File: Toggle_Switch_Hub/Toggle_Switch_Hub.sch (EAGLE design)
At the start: 6 parts

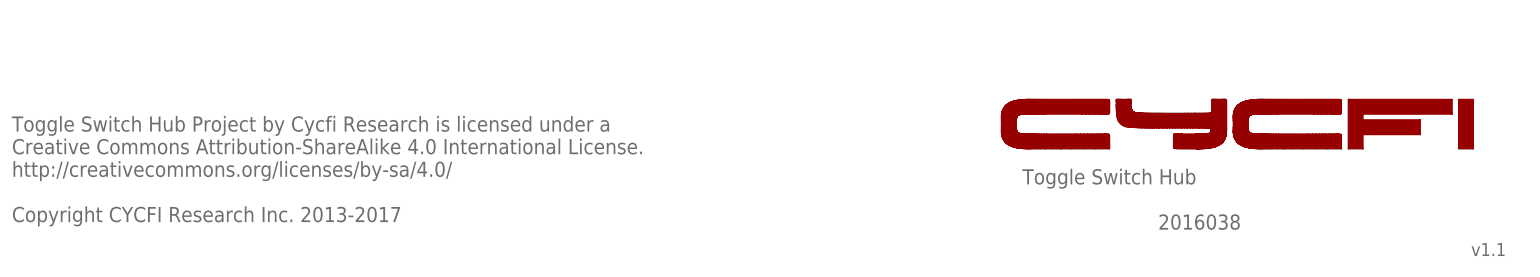
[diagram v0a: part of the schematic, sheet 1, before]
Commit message: Updated BOM and Document Number
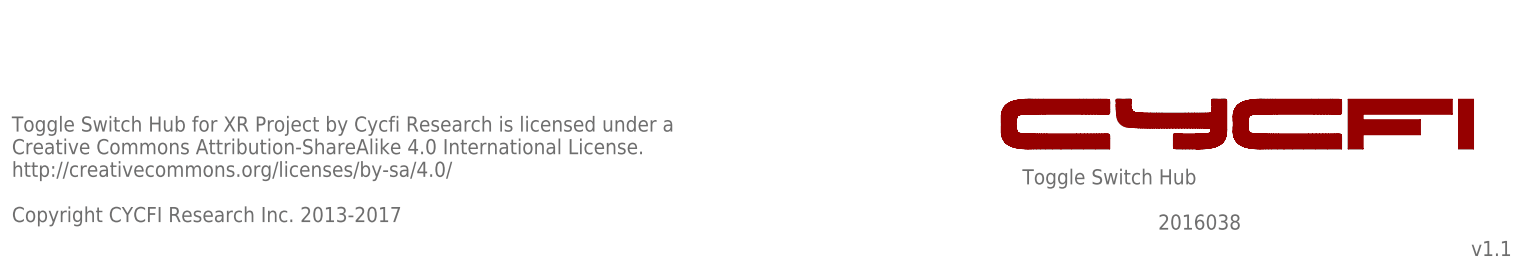
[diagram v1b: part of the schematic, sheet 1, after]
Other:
- note added: "Toggle Switch Hub for XR Project by Cycfi Research is licensed under a Creative Commons Attribution-ShareAlike 4.0 International License. http://creativecommons.org/licenses/by-sa/4.0/ Copyright CYCFI Research Inc. 2013-2017"
- note removed: "Toggle Switch Hub Project by Cycfi Research is licensed under a Creative Commons Attribution-ShareAlike 4.0 International License. http://creativecommons.org/licenses/by-sa/4.0/ Copyright CYCFI Research Inc. 2013-2017"
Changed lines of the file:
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@@
 <?xml version="1.0" encoding="utf-8"?>
 <!DOCTYPE eagle SYSTEM "eagle.dtd">
-<eagle version="6.3">
+<eagle version="7.6.0">
 <drawing>
 <settings>
@@
 GND</text>
 <text x="177.8" y="19.05" size="2.54" layer="95" font="vector">Toggle Switch Hub</text>
-<text x="253.365" y="6.985" size="2.1844" layer="95">v1.1</text>
-<text x="7.62" y="12.7" size="2.54" layer="95">Toggle Switch Hub Project by Cycfi Research is licensed under a
+<text x="253.365" y="6.985" size="2.54" layer="95">v1.1</text>
+<text x="7.62" y="12.7" size="2.54" layer="95">Toggle Switch Hub for XR Project by Cycfi Research is licensed under a
 Creative Commons Attribution-ShareAlike 4.0 International License.
 http://creativecommons.org/licenses/by-sa/4.0/
@@
 <text x="193.675" y="94.615" size="1.778" layer="95">INS</text>
 <text x="178.435" y="19.685" size="2.54" layer="95">Toggle Switch Hub</text>
-<text x="254" y="7.62" size="2.1844" layer="95">v1.1</text>
-<text x="8.255" y="13.335" size="2.54" layer="95">Toggle Switch Hub Project by Cycfi Research is licensed under a
+<text x="254" y="7.62" size="2.54" layer="95">v1.1</text>
+<text x="8.255" y="13.335" size="2.54" layer="95">Toggle Switch Hub for XR Project by Cycfi Research is licensed under a
 Creative Commons Attribution-ShareAlike 4.0 International License.
 http://creativecommons.org/licenses/by-sa/4.0/
